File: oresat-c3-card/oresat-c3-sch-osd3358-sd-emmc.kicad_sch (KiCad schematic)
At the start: 52 parts, among them J5 DM3BT-DSF-PEJS, U1 OSD3358-1G-ISM, U42 74LVC2G34, U8 TCAN330, U9 SFEM016GB1EA1TO-I-GE-121-STD

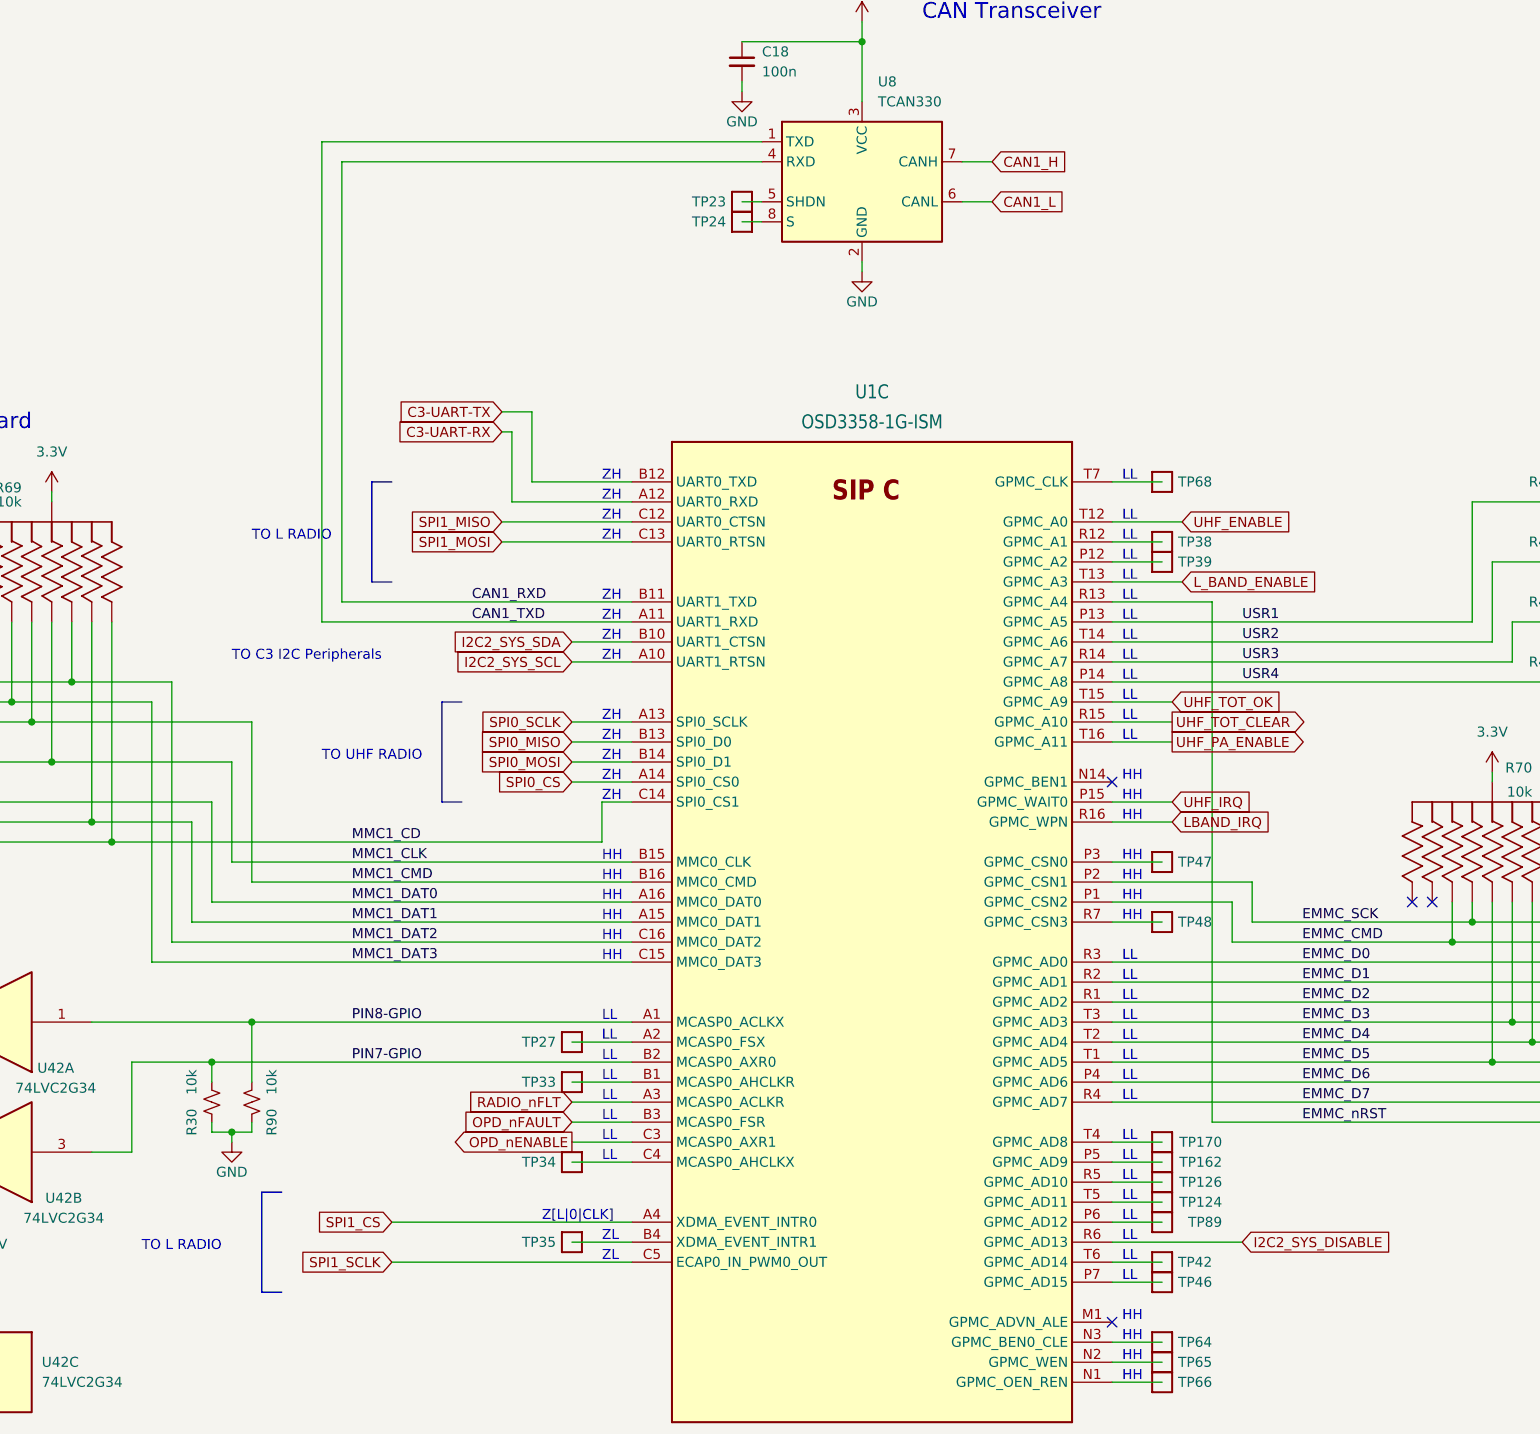
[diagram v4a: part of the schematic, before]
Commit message: Minor polishing on schematic, mostly text notes.
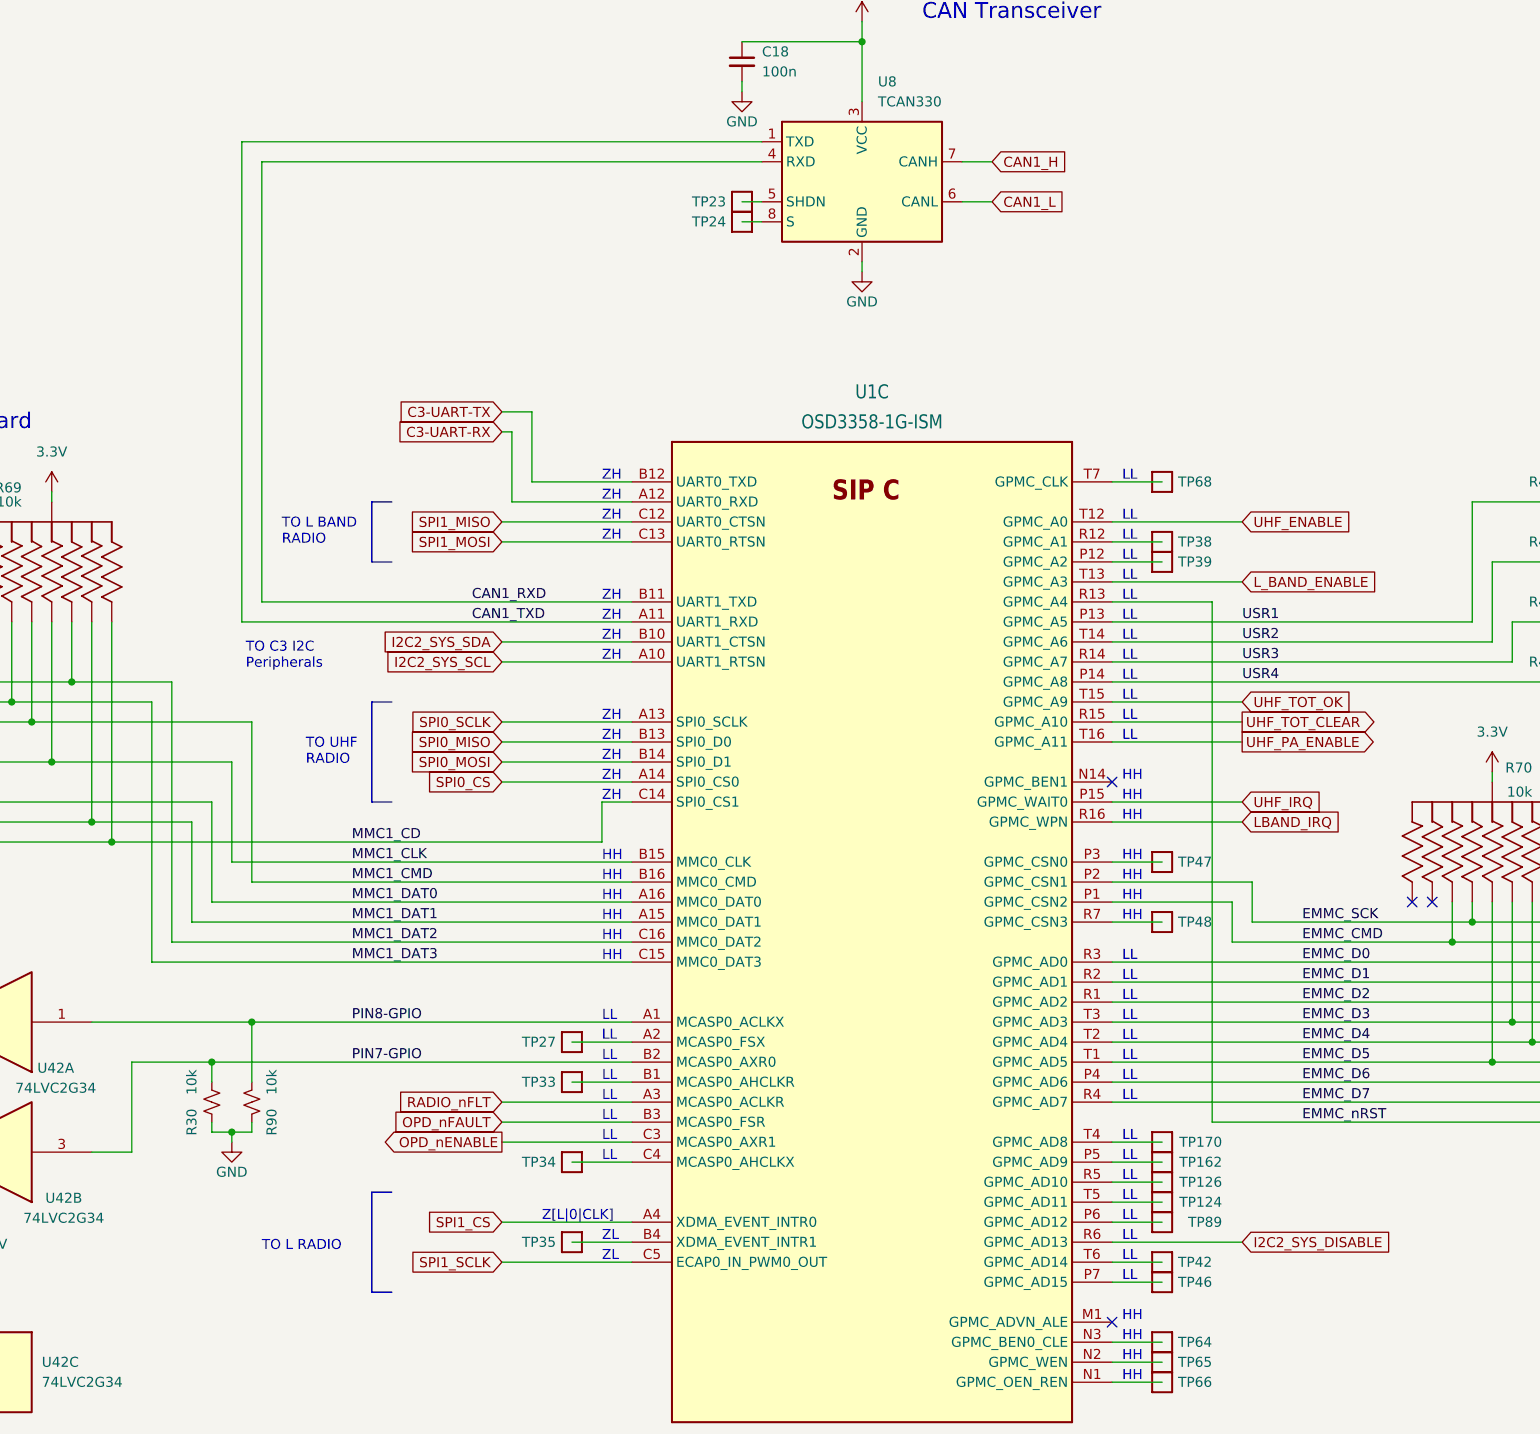
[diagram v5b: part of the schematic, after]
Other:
- note added: "TO L BAND RADIO"

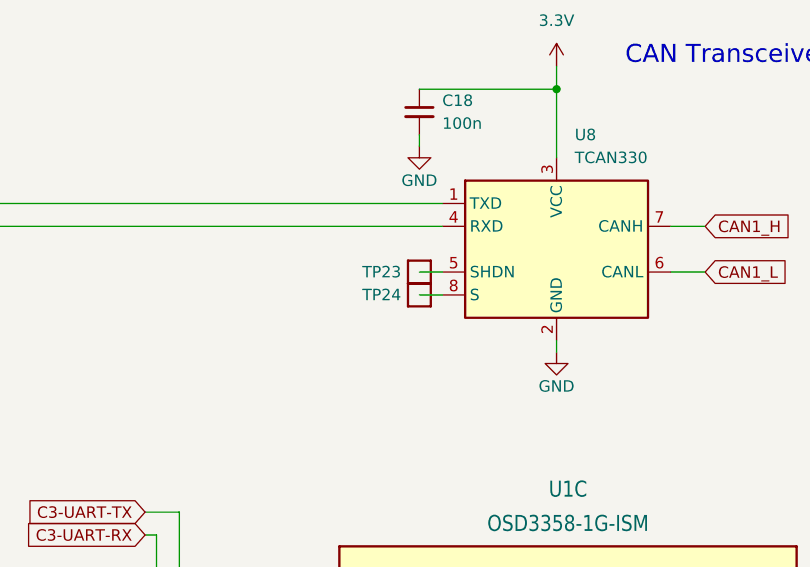
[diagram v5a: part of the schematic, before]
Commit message: Added L band ground cut (Glenn's fault). DRC errrors due to 50 ohm clearance; investigating custom rules now.
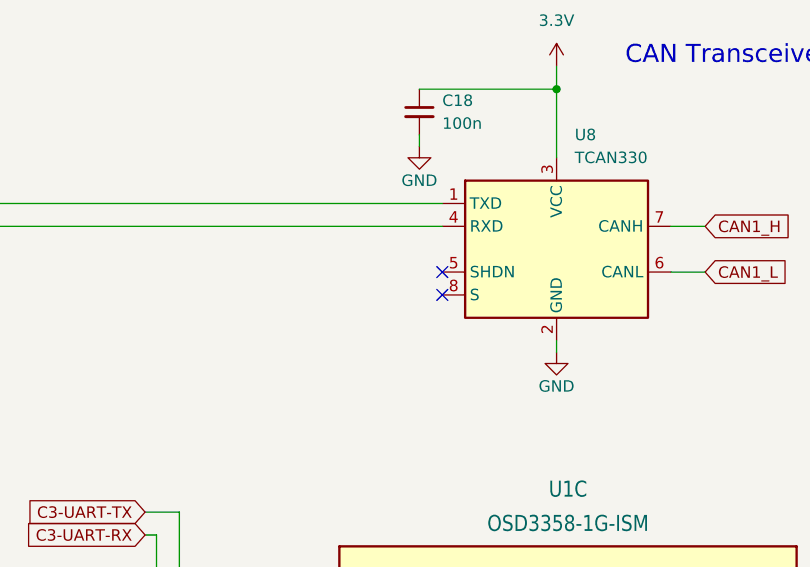
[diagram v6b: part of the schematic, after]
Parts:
- removed TP23, TP24: Test-Point, oresat-misc:TestPoint_Pad_D1.0mm, symbol oresat-misc:Test-Point-1mm-round
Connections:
- no-connect marks 8 -> 10
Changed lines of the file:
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@@
 		(at 223.52 139.7)
 	)
+	(no_connect
+		(at 179.07 68.58)
+	)
+	(no_connect
+		(at 179.07 66.04)
+	)
 	(wire
 		(pts
@@
 	(wire
 		(pts
-			(xy 176.53 68.58) (xy 179.07 68.58)
-		)
-		(stroke
-			(width 0)
-			(type default)
-		)
-	)
-	(wire
-		(pts
 			(xy 276.86 154.94) (xy 276.86 172.72)
 		)
@@
 	(wire
 		(pts
-			(xy 176.53 66.04) (xy 179.07 66.04)
-		)
-		(stroke
-			(width 0)
-			(type default)
-		)
-	)
-	(wire
-		(pts
 			(xy 73.66 144.78) (xy 93.98 144.78)
 		)
@@
 	)
 	(symbol
-		(lib_id "oresat-misc:Test-Point-1mm-round")
-		(at 176.53 66.04 0)
-		(unit 1)
-		(exclude_from_sim yes)
-		(in_bom no)
-		(on_board yes)
-		(dnp no)
-		(property "Reference" "TP23"
-			(at 170.18 66.04 0)
-			(effects
-				(font
-					(size 1.27 1.27)
-				)
-				(justify left)
-			)
-		)
-		(property "Value" "Test-Point"
-			(at 176.53 63.5 0)
-			(effects
-				(font
-					(size 1.27 1.27)
-				)
-				(hide yes)
-			)
-		)
-		(property "Footprint" "oresat-misc:TestPoint_Pad_D1.0mm"
-			(at 176.53 55.88 0)
-			(effects
-				(font
-					(size 1.27 1.27)
-				)
-				(hide yes)
-			)
-		)
-		(property "Datasheet" ""
-			(at 176.53 66.04 0)
-			(effects
-				(font
-					(size 1.27 1.27)
-				)
-				(hide yes)
-			)
-		)
-		(property "Description" "1mm round SMT test point"
-			(at 176.53 66.04 0)
-			(effects
-				(font
-					(size 1.27 1.27)
-				)
-				(hide yes)
-			)
-		)
-		(pin "1"
-		)
-		(instances
-			(project "oresat-c3"
-				(path "/65d12cdd-c326-4033-9053-c59fa4e0b25e/f3d147ad-4cea-4d77-ae60-95882b03454e"
-					(reference "TP23")
-					(unit 1)
-				)
-			)
-		)
-	)
-	(symbol
 		(lib_id "power:GND")
 		(at 350.52 154.94 0)
@@
 					(unit 1)
 				)
-			)
-		)
-	)
-	(symbol
-		(lib_id "oresat-misc:Test-Point-1mm-round")
-		(at 176.53 68.58 0)
-		(unit 1)
-		(exclude_from_sim yes)
-		(in_bom no)
-		(on_board yes)
-		(dnp no)
-		(property "Reference" "TP24"
-			(at 170.18 68.58 0)
-			(effects
-				(font
-					(size 1.27 1.27)
-				)
-				(justify left)
-			)
-		)
-		(property "Value" "Test-Point"
-			(at 176.53 66.04 0)
-			(effects
-				(font
-					(size 1.27 1.27)
-				)
-				(hide yes)
-			)
-		)
-		(property "Footprint" "oresat-misc:TestPoint_Pad_D1.0mm"
-			(at 176.53 58.42 0)
-			(effects
-				(font
-					(size 1.27 1.27)
-				)
-				(hide yes)
-			)
-		)
-		(property "Datasheet" ""
-			(at 176.53 68.58 0)
-			(effects
-				(font
-					(size 1.27 1.27)
-				)
-				(hide yes)
-			)
-		)
-		(property "Description" "1mm round SMT test point"
-			(at 176.53 68.58 0)
-			(effects
-				(font
-					(size 1.27 1.27)
-				)
-				(hide yes)
-			)
-		)
-		(pin "1"
-		)
-		(instances
-			(project "oresat-c3"
-				(path "/65d12cdd-c326-4033-9053-c59fa4e0b25e/f3d147ad-4cea-4d77-ae60-95882b03454e"
-					(reference "TP24")
-					(unit 1)
-				)

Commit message: Fixed BOM issue with eMMC
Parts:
- U9: DPN 3052-FDMM032GBE-3101-ND -> 557-MTFC32GAZAQHD-IT-ND; MFR Flexxon Pte Ltd -> Micron Technology Inc.; MPN FDMM032GBE-3101 -> MTFC32GAZAQHD-IT
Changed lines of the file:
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@@
 			)
 		)
-		(property "Datasheet" "https://www.flexxon.com/wp-content/uploads/Flexxon%20Profile/Flexxon-Brochure-Jan2020_compressed.pdf"
+		(property "Datasheet" "https://www.micron.com/products/managed-nand/emmc/part-catalog/mtfc32gazaqhd-it?login"
 			(at 330.2 175.26 0)
 			(effects
@@
 			)
 		)
-		(property "Description" "Memory Card microSD™ 32GB UHS Class 1 TLC"
+		(property "Description" "FLASH - NAND Memory IC 256Gbit eMMC 200 MHz 153-VFBGA (11.5x13)"
 			(at 330.2 175.26 0)
 			(effects
@@
 			)
 		)
-		(property "DPN" "3052-FDMM032GBE-3101-ND"
+		(property "DPN" "557-MTFC32GAZAQHD-IT-ND"
 			(at 330.2 175.26 0)
 			(effects
@@
 			)
 		)
-		(property "MFR" "Flexxon Pte Ltd"
+		(property "MFR" "Micron Technology Inc."
 			(at 330.2 175.26 0)
 			(effects
@@
 			)
 		)
-		(property "MPN" "FDMM032GBE-3101"
+		(property "MPN" "MTFC32GAZAQHD-IT"
 			(at 330.2 175.26 0)
 			(effects
